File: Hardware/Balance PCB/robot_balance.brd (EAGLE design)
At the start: 100 x 50 mm, 54 parts, among them P1 10118194-0001LF, Q1 16Mhz

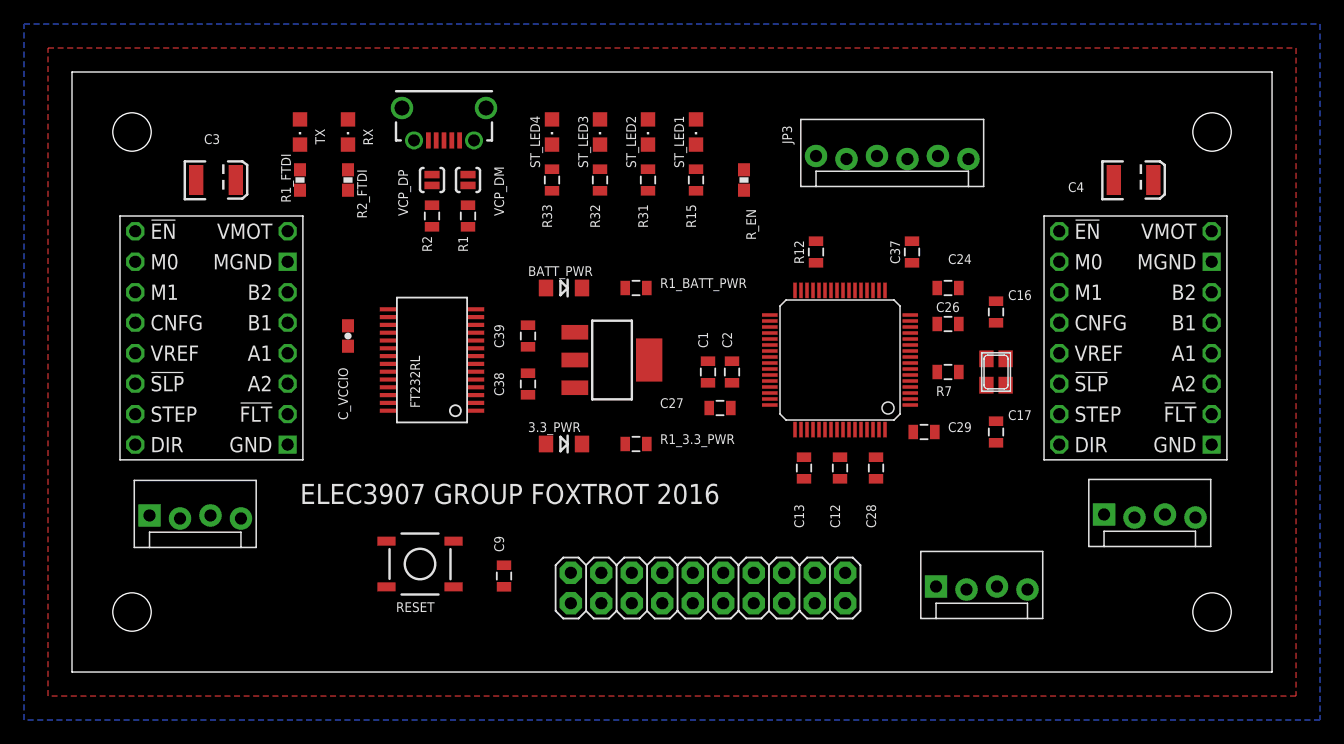
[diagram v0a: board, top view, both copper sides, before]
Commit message: Moved MPU to middle of board
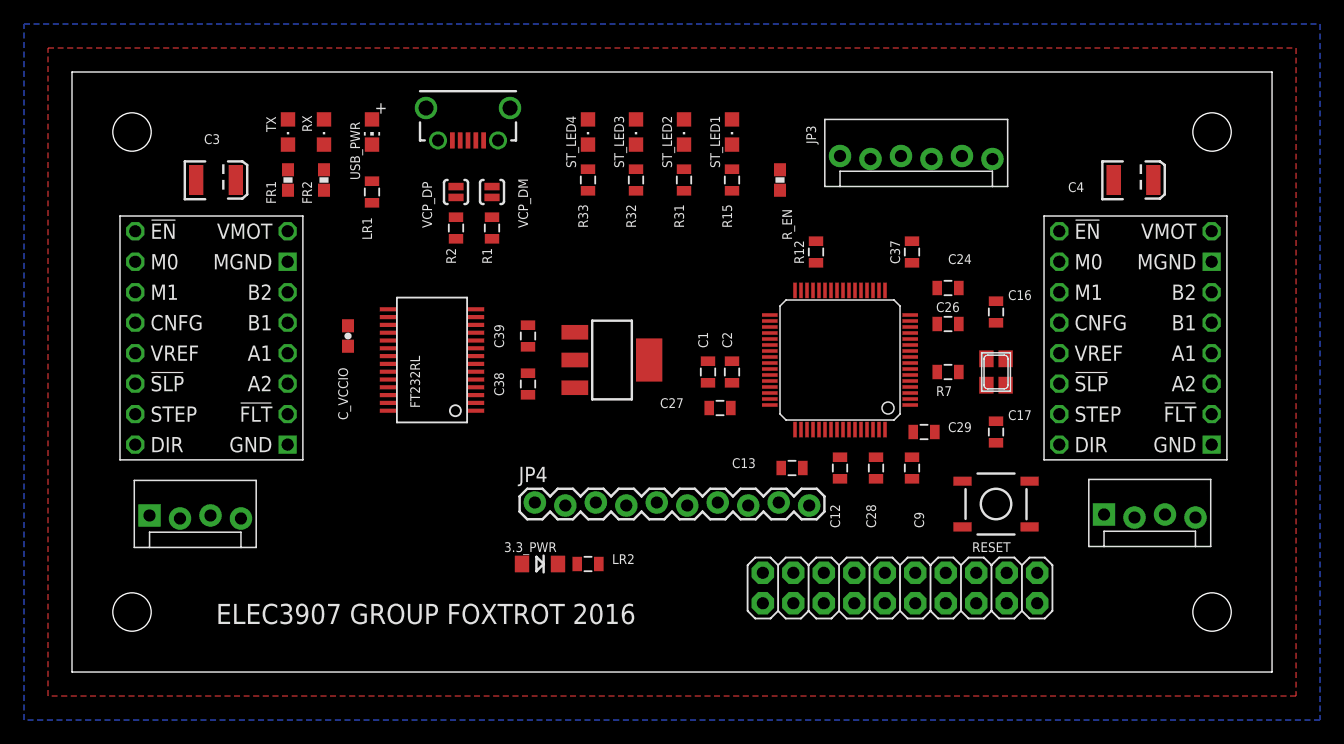
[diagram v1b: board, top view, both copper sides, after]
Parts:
- removed BATT_PWR: (no value), LilyPad-Wearables:LED-1206
- removed JP5: (no value), SparkFun-Connectors:MOLEX-1X4_LOCK
- removed R1_3.3_PWR: 1K, SparkFun-Resistors:0805
- removed R1_BATT_PWR: 1k, SparkFun-Resistors:0805
- removed R1_FTDI, R2_FTDI: 1K, SparkFun-Passives:0603-RES
- added FR1, FR2: 1K, SparkFun-Passives:0603-RES
- added JP4: M10LOCK, SparkFun-Connectors:1X10_LOCK
- added LR1: 1k, SparkFun-Resistors:0805
- added LR2: 1K, SparkFun-Resistors:0805
- added USB_PWR: (no value), adafruit:CHIP-LED0805
- moved RESET 48.3 mm to (77.0, 14.0)
- moved C9 35.2 mm to (70.0, 17.0), turned to 270 degrees
- moved U$2 16.0 mm to (69.0, 7.00)
- moved 3.3_PWR 10.2 mm to (39.0, 9.00)
- moved R15 3.00 mm to (55.0, 41.0)
- moved R31 3.00 mm to (51.0, 41.0)
- moved R32 3.00 mm to (47.0, 41.0)
- moved R33 3.00 mm to (43.0, 41.0)
- moved R_EN 3.00 mm to (59.0, 41.0)
- moved ST_LED1 3.00 mm to (55.0, 45.0)
- moved ST_LED2 3.00 mm to (51.0, 45.0)
- moved ST_LED3 3.00 mm to (47.0, 45.0)
- moved ST_LED4 3.00 mm to (43.0, 45.0)
- moved R1 2.24 mm to (35.0, 37.0)
- moved R2 2.24 mm to (32.0, 37.0)
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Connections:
- new net INT: JP4.8, U$4.57
- net 5V: now also JP4.1, USB_PWR.A; no longer BATT_PWR.A, JP5.3
- net GND: now also JP4.2, LR1.1, LR2.1; no longer JP5.4, R1_3.3_PWR.1, R1_BATT_PWR.1
- net IMU_SCL: now also JP4.3; no longer JP5.1
- net IMU_SDA: now also JP4.4; no longer JP5.2
- net N$10: now also FR2.2; no longer R2_FTDI.2
- net N$11: now also FR2.1; no longer R2_FTDI.1
- net N$18: now also LR2.2; no longer R1_3.3_PWR.2
- net N$19: now also LR1.2, USB_PWR.C; no longer BATT_PWR.C, R1_BATT_PWR.2
- net N$8: now also FR1.1; no longer R1_FTDI.1
- net N$9: now also FR1.2; no longer R1_FTDI.2

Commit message: layout
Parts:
- 3.3_PWR: device LilyPad-Wearables:LED-1206 -> adafruit:CHIPLED_0805
- moved R12 18.2 mm to (65.0, 17.0), turned to 90 degrees
- moved C12 18.0 mm to (63.0, 35.0), turned to 90 degrees
- moved C13 16.3 mm to (57.0, 33.0)
- moved LR2 10.6 mm to (35.0, 16.0), turned to 270 degrees
- moved 3.3_PWR 9.90 mm to (32.0, 16.0), turned to 180 degrees
- moved JP4 9.26 mm to (38.6, 4.74)
- moved U$2 8.06 mm to (77.0, 6.00)
- moved C37 3.00 mm to (67.0, 35.0)
- moved C24 2.00 mm to (71.0, 32.0)
- moved LR1 1.41 mm to (26.0, 41.0)
- moved C28 1.00 mm to (68.0, 17.0)
- moved C9 1.00 mm to (71.0, 17.0)
- moved RESET 1.00 mm to (78.0, 14.0)
- moved USB_PWR 1.00 mm to (26.0, 45.0)

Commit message: route
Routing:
- net 3.3V: track 0.00 -> 127.0 mm, vias 0 -> 9
- net 5V: track 0.00 -> 125.4 mm, vias 0 -> 1
- net !S1_ENABLE: track 0.00 -> 102.2 mm, vias 0 -> 2
- net !S1_SLEEP: track 0.00 -> 97.2 mm, vias 0 -> 2
- net LED3: track 0.00 -> 93.9 mm
- net S1_M0: track 0.00 -> 93.0 mm, vias 0 -> 2
- net V_USB: track 0.00 -> 90.5 mm, vias 0 -> 1
- net S1_STEP: track 0.00 -> 89.8 mm, vias 0 -> 2
- net S1_M1: track 0.00 -> 87.9 mm, vias 0 -> 2
- net S1_DIR: track 0.00 -> 84.1 mm, vias 0 -> 2
- net !S1_FAULT: track 0.00 -> 67.4 mm, vias 0 -> 1
- net S2_DIR: track 0.00 -> 62.5 mm
- net !S2_FAULT: track 0.00 -> 55.0 mm, vias 0 -> 3
- net SWO: track 0.00 -> 51.3 mm
- net LED4: track 0.00 -> 49.0 mm, vias 0 -> 4
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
